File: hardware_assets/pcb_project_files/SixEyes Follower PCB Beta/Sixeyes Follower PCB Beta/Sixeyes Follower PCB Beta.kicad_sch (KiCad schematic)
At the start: 19 parts, among them J1 Micro_SD_Card, J10 Conn_01x03_Pin, J11 Conn_01x03_Pin, J12 Conn_01x02_Pin, J2 Conn_01x04_Pin, J3 Conn_01x04_Pin, J4 Conn_01x04_Pin, J5 Conn_01x04_Pin, J6 Conn_01x04_Pin, J7 Conn_01x02_Pin, J8 Conn_01x02_Pin, J9 Conn_01x03_Pin, U1 ESP32-S3-WROOM-1, U2 TMC2209-LA, U3 TMC2209-LA, U4 TMC2209-LA, U5 TMC2209-LA, U6 MIC5219-3.3YM5, U7 CH340K

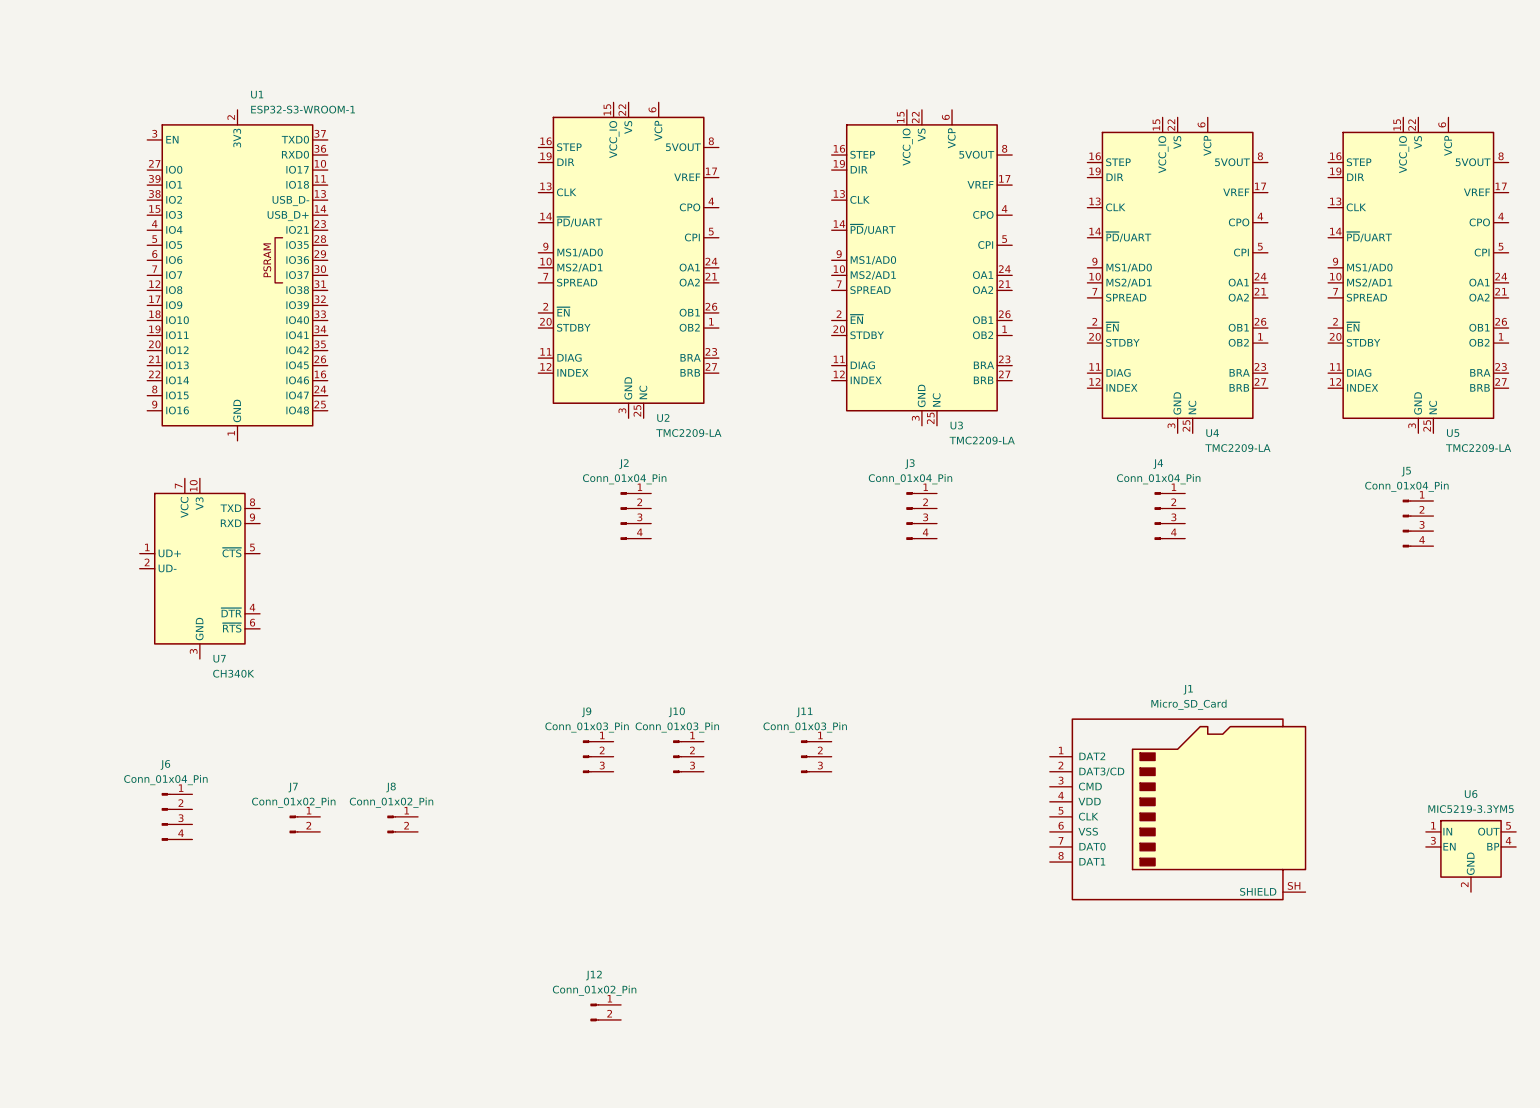
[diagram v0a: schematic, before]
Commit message: feat: add Beta PCB schematic symbols, 3D models, custom footprints; update README
Schematic (Sixeyes Follower PCB Beta.kicad_sch):
- Add TPS54540B (6.6V sync buck) symbol and instance U8
- Add LMR14030S (5.0V async buck) symbol and instance U9
- Add USB_C_Receptacle_USB2.0 symbols for J13 (J_USB1, native OTG) and J14 (J_USB2, CH340K)
- Add Conn_01x02_Pin instance J15 (J_LDR_PWR, Node1 5V/GND power, separate from J6 signals)
- All symbols reference correct footprints and datasheets per Beta Rev2 design spec

Hardware assets:
- Add 3D models: TMC2209, TPS54540B, LMR14030S, USB-C, XT30, Molex 2/3/4-pin
- Add CustomFootprints.pretty with sanka.kicad_mod and sanka2.kicad_mod
- Add docs/references/Sixeyes Node0 (Folloer PCB Beta).txt (Beta Rev2 design spec)

README.md:
- Fix GitHub org (SixEyes-Open-Source → studiosanka)
- Fix firmware structure to show alpha/beta split
- Fix hardware_assets paths (pcb_project_files, pcb_latest_gerber)
- Add Alpha vs Beta hardware generation comparison table
- Update build commands to target firmware/alpha and firmware/beta
- Add Beta PCB to Project Status
- Update Last Updated to June 2026

Co-Authored-By: Claude Sonnet 4.6 <noreply@anthropic.com>
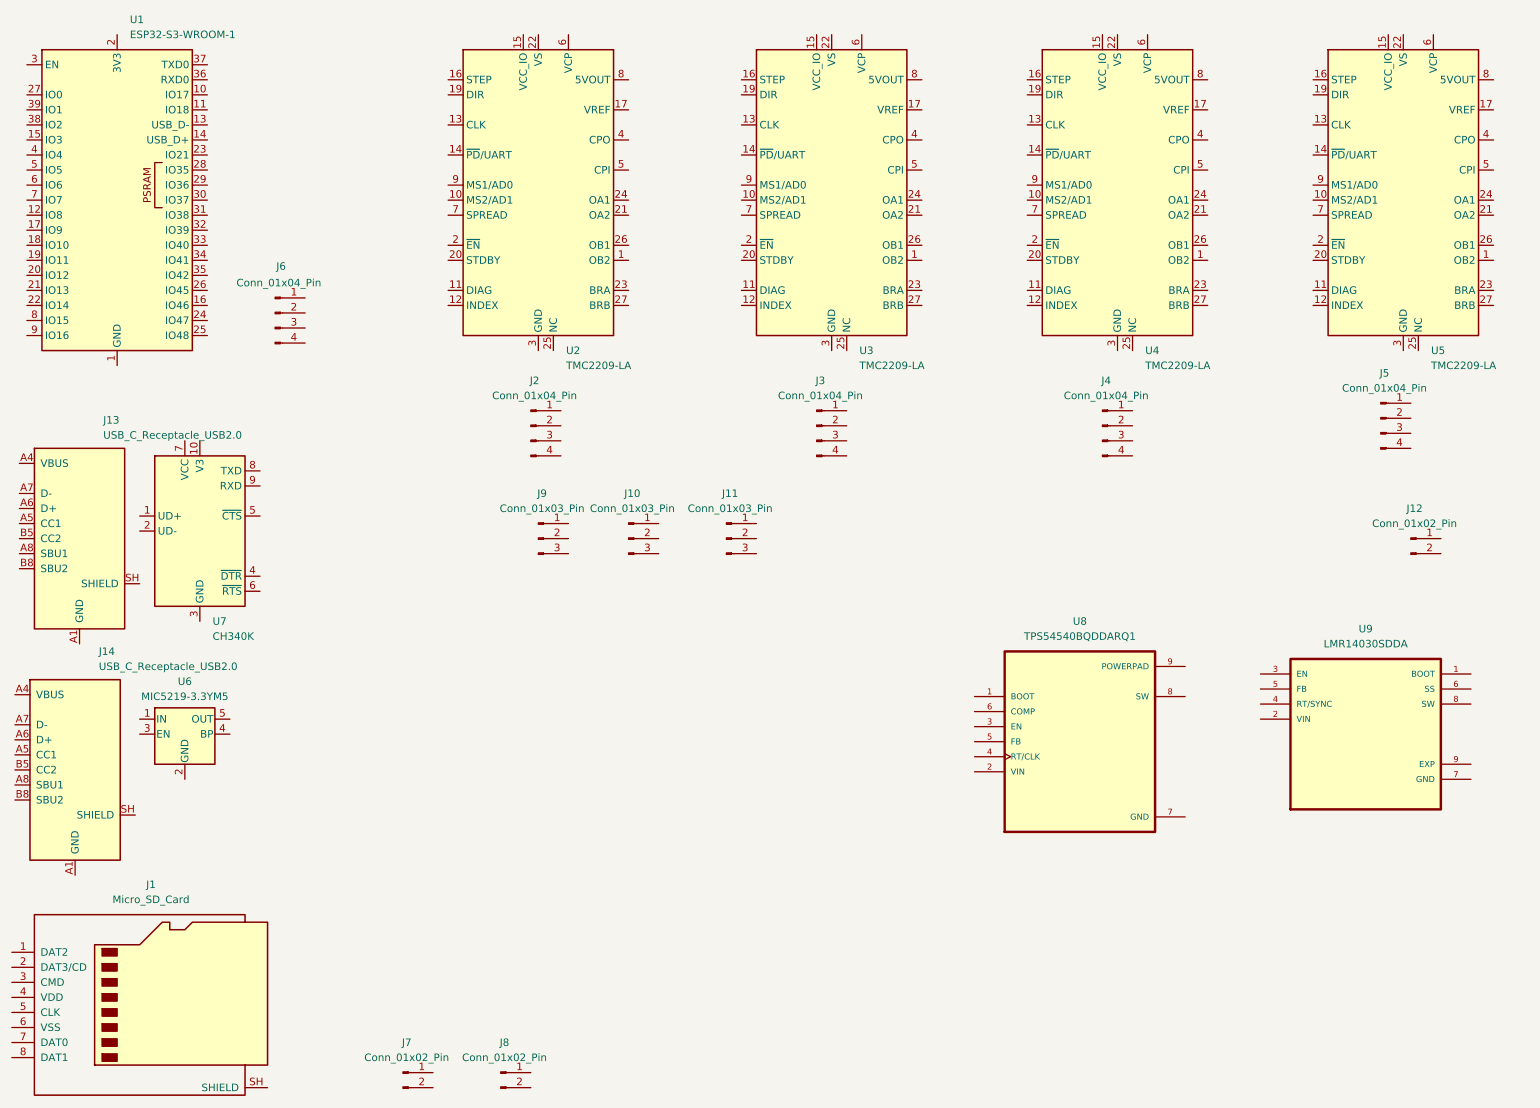
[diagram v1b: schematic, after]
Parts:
- added J13, J14: USB_C_Receptacle_USB2.0, Connector_USB:USB_C_Receptacle_HRO_TYPE-C-31-M-12, symbol Connector_USB:USB_C_Receptacle_USB2.0
- added U8: TPS54540BQDDARQ1, TPS54540BQDDARQ1:VREG_LM5017MR_NOPB, symbol TPS54540BQDDARQ1:TPS54540BQDDARQ1
- added U9: LMR14030SDDA, LMR14030SDDA:VREG_LM5017MR_NOPB, symbol LMR14030SDDA:LMR14030SDDA
- J10, J11, J9: footprint (none) -> Connector_JST:JST_XH_B3B-XH-A_1x03_P2.50mm_Vertical
- J2, J3, J4, J5, J6: footprint (none) -> Connector_JST:JST_XH_B4B-XH-A_1x04_P2.50mm_Vertical
- J7, J8: footprint (none) -> Connector_JST:JST_XH_B2B-XH-A_1x02_P2.50mm_Vertical
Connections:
- new net EXP: U9.9 (EXP), U9.V1 (EXP), U9.V2 (EXP), U9.V3 (EXP), U9.V4 (EXP), U9.V5 (EXP), U9.V6 (EXP)
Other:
- moved on the sheet: J1, J10, J11, J12, J2, J3, J4, J5, J6, J7, J8, J9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
